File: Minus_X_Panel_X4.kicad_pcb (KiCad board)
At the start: 2 copper layers, 1 part, among them J1 SM05B-SRSS-TB_LF__SN_

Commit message: Symbol and foot print id almost ready
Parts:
- removed J1: SM05B-SRSS-TB_LF__SN_, Custom-Footprints:JST_SM05B-SRSS-TB_LF__SN_
- added D1: CUHS20S30,H3F, Custom-Footprints:CUHS20S30,H3F, B.Cu at (237.2, 135.3)
- added D2: CUHS20S30,H3F, Custom-Footprints:CUHS20S30,H3F, B.Cu at (239.4, 181.0)
- added D3: CUHS20S30,H3F, Custom-Footprints:CUHS20S30,H3F, B.Cu at (165.0, 193.3)
- added D4: CUHS20S30,H3F, Custom-Footprints:CUHS20S30,H3F, B.Cu at (237.0, 45.8)
- added S1: solar_cell_B, Custom-Footprints:solar_cell_B, F.Cu at (162.1, 75.4)
- added S2: Solar_cell_C, Custom-Footprints:solar_cell_C, F.Cu at (162.1, 165.4)
- added S3: Solar_cell_C, Custom-Footprints:solar_cell_C, F.Cu at (162.1, 231.8)
- added S4: solar_cell_B, Custom-Footprints:solar_cell_B, F.Cu at (162.1, 120.4)
- added U$1: 2PIN_FEMALE, Custom-Footprints:FSR-41057-02-F, B.Cu at (236.2, 80.4)
- added U$2: 3PIN_FEMALE_-XC3PIN_MALE, Custom-Footprints:FSR-41057-03-F, B.Cu at (236.8, 192.8)
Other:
- board outline added: 82.9 x 214.9 mm
- board text added: "For Instructional Use Only."
- board text added: "SOLIDWORKS Educational Product."

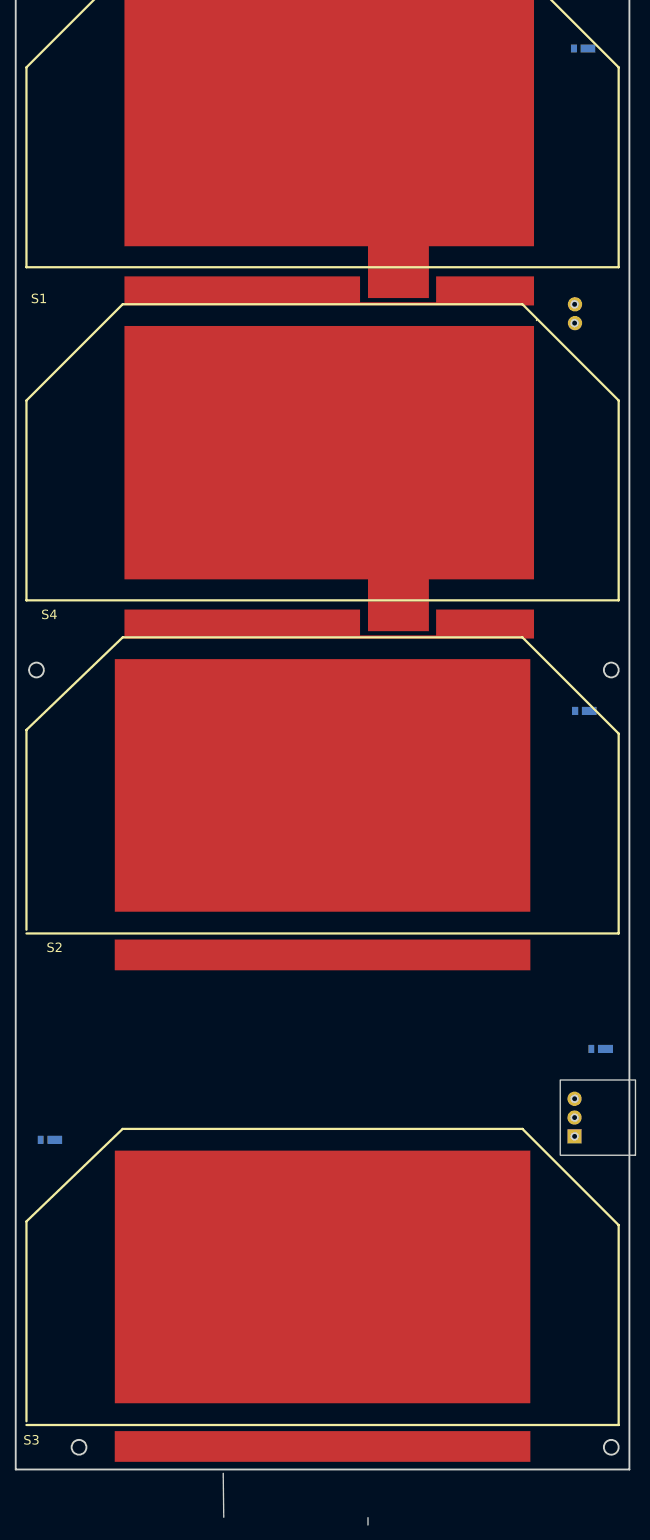
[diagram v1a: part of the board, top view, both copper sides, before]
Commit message: i updateed the PCB configuration of the panel
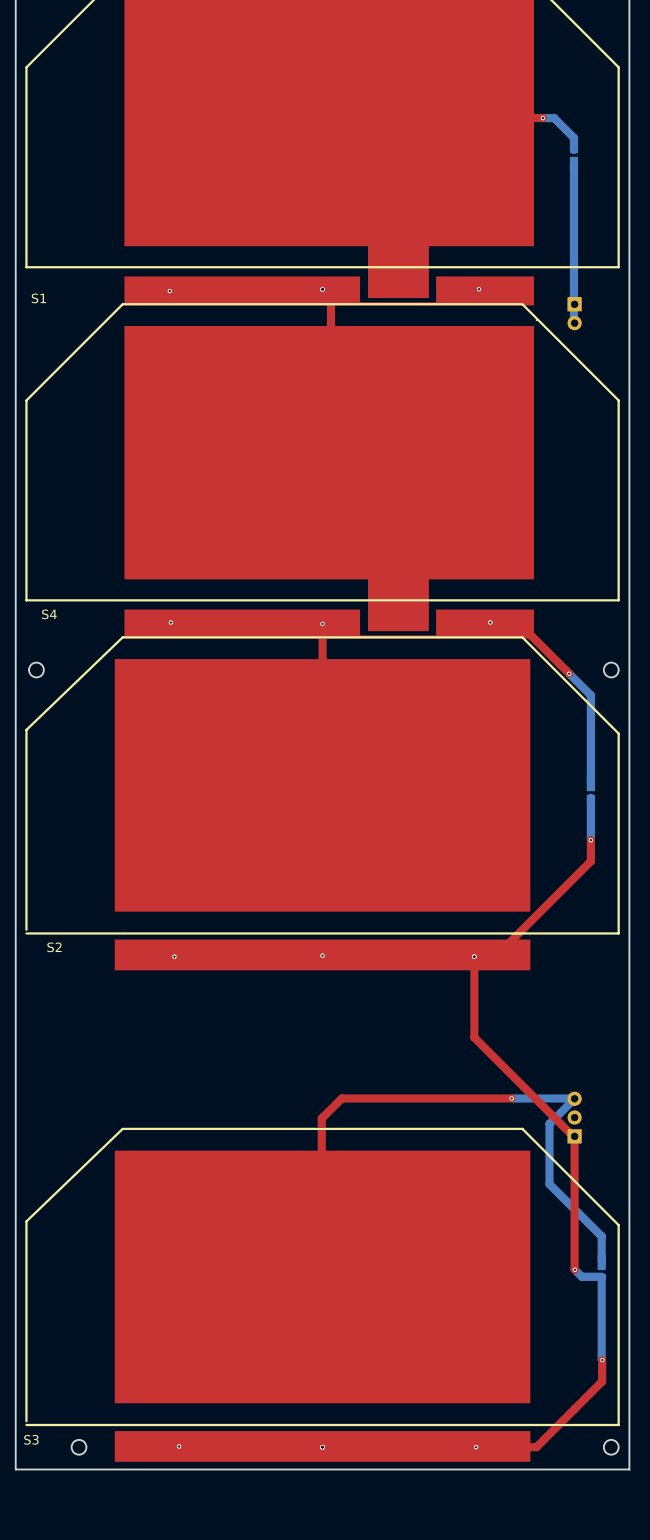
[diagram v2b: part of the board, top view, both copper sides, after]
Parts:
- removed D3: CUHS20S30,H3F, Custom-Footprints:CUHS20S30,H3F
- removed U$1: 2PIN_FEMALE, Custom-Footprints:FSR-41057-02-F
- removed U$2: 3PIN_FEMALE_-XC3PIN_MALE, Custom-Footprints:FSR-41057-03-F
- added U$3: 3PIN_FEMALE_-XC3PIN_MALE, Custom-Footprints:FSR-41057-03-F, B.Cu at (236.2, 192.8)
- added U$4: 2PIN_FEMALE, Custom-Footprints:FSR-41057-02-F, B.Cu at (236.2, 80.4)
- moved D2 29.8 mm to (239.8, 210.8), turned to -90 degrees
- moved D4 14.7 mm to (236.1, 60.5), turned to 90 degrees
- moved D1 10.8 mm to (238.4, 146.1), turned to -90 degrees
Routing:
- net GND: track 0.00 -> 116.9 mm, vias 0 -> 14
- net Net-(D2-K): track 0.00 -> 83.2 mm, vias 0 -> 1
- net Net-(D1-K): track 0.00 -> 45.1 mm, vias 0 -> 4
- net Net-(D4-A): track 0.00 -> 35.6 mm, vias 0 -> 1
- net Net-(S1-PadGND): track 0.00 -> 22.3 mm, vias 0 -> 6
- net Net-(D4-K): track 0.00 -> 21.5 mm
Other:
- board size 82.9 x 214.9 mm -> 82.9 x 207.4 mm
- board text removed: "For Instructional Use Only."
- board text removed: "SOLIDWORKS Educational Product."

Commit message: -X Panel last updated the tracks
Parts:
- moved D2 71.0 mm to (168.9, 207.1), turned to 180 degrees
- moved D4 11.6 mm to (236.1, 72.1)
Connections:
- net Net-(D1-K) renamed /+VA
- net Net-(D2-K) renamed /+VD
- net Net-(D4-A) renamed /+VC
- net Net-(S1-PadGND) renamed /+VB
- U$3 pad 1GND: (no net) -> GND
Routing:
- net /+VB: track 22.3 -> 236.3 mm, vias 6 -> 9
- net /+VA: track 45.1 -> 237.7 mm, vias 4 -> 9
- net /+VC: track 35.6 -> 158.0 mm, vias 1 -> 6
- net /+VD: track 83.2 -> 198.6 mm, vias 1 -> 7
- net Net-(D4-K): track 21.5 -> 10.0 mm
- net GND: track 116.9 -> 115.0 mm, vias 14 -> 7
- added copper zone on B.Cu, net /+VA
- added copper zone on B.Cu, net /+VB
- added copper zone on B.Cu, net /+VC
- added copper zone on B.Cu, net /+VD
- added copper zone on B.Cu, net GND
- added copper zone on F.Cu, net GND

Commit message: footprint of the Panel is modified with tracking
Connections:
- net /+VA renamed /+V4A
- net /+VB renamed /+V4B
- net /+VC renamed /+V4C
- net /+VD renamed /+V4D
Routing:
- net /+V4D: track 198.6 -> 179.9 mm
- net GND: track 115.0 -> 110.5 mm

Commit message: Updated the Pin Configuration
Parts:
- moved U$4 87.7 mm to (150.4, 98.8), turned to -90 degrees
- moved U$3 87.2 mm to (150.4, 208.5)
- moved D4 85.6 mm to (150.5, 69.0)
- moved D2 51.2 mm to (219.9, 211.7), turned to -90 degrees
- moved S1 23.7 mm to (144.5, 91.2)
- moved S2 23.7 mm to (144.5, 181.2)
- moved S4 23.7 mm to (144.5, 136.2)
- moved S3 23.7 mm to (144.5, 247.5)
- moved D1 21.5 mm to (217.0, 143.7)
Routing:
- net /+V4D: track 179.9 -> 229.3 mm, vias 7 -> 6
- net Net-(D4-K): track 10.0 -> 29.2 mm
- net GND: track 110.5 -> 91.7 mm, vias 7 -> 14
- net /+V4C: track 158.0 -> 166.4 mm, vias 6 -> 7
- net /+V4B: track 236.3 -> 243.6 mm, vias 9 -> 10
- net /+V4A: track 237.7 -> 244.9 mm
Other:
- board size 82.9 x 207.4 mm -> 82.9 x 207.3 mm
- board text added: "For Instructional Use Only."
- board text added: "GND"
- board text added: "PWR"
- board text added: "PWR-4p*"
- board text added: "SOLIDWORKS Educational Product."
